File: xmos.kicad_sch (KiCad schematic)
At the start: 69 parts, among them Q1 LBSS138WT1G, Q2 BC847B, Q3 LBSS138WT1G, U10 SN74LVC125APWR, U7 XU316-1024-QF60B-C24, U8 W25Q128JVSIQ, U9 TLV73333PDBVR, Y2 24MHz

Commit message: rev2 update
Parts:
- C92: Dielectric (none) -> X5R; Supplier Part (none) -> C1525
- Q1: Manufacturer LRC(乐山无线电) -> LRC
- Q3: Current (none) -> 200mA; Manufacturer Part (none) -> LBSS138WT1G; Supplier Part (none) -> C383201
- R33: Function (none) -> XMOS; Manufacturer YAGEO -> UNI-ROYAL(Uniroyal Elec); Manufacturer Part (none) -> 0402WGF4703TCE; Supplier Part (none) -> C25790
- R34: Function (none) -> XMOS; Manufacturer YAGEO -> UNI-ROYAL(Uniroyal Elec); Manufacturer Part (none) -> 0402WGF1002TCE; Supplier Part (none) -> C25744
- R63: Function (none) -> XMOS; Manufacturer YAGEO -> UNI-ROYAL(Uniroyal Elec); Manufacturer Part (none) -> 0402WGF1000TCE; Supplier Part (none) -> C25076
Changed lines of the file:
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@@
 			)
 		)
-		(property "Manufacturer" "YAGEO"
+		(property "Manufacturer" "UNI-ROYAL(Uniroyal Elec)"
 			(at 144.78 151.13 0)
 			(effects
@@
 			)
 		)
+		(property "Manufacturer Part" "0402WGF1002TCE"
+			(at 144.78 151.13 90)
+			(effects
+				(font
+					(size 1.27 1.27)
+				)
+				(hide yes)
+			)
+		)
+		(property "Supplier Part" "C25744"
+			(at 144.78 151.13 90)
+			(effects
+				(font
+					(size 1.27 1.27)
+				)
+				(hide yes)
+			)
+		)
+		(property "Function" "XMOS"
+			(at 144.78 151.13 90)
+			(effects
+				(font
+					(size 1.27 1.27)
+				)
+				(hide yes)
+			)
+		)
 		(pin "1"
 		)
@@
 			)
 		)
-		(property "Dielectric" ""
+		(property "Dielectric" "X5R"
 			(at 144.78 165.1 0)
 			(effects
@@
 			)
 		)
+		(property "Supplier Part" "C1525"
+			(at 144.78 165.1 0)
+			(effects
+				(font
+					(size 1.27 1.27)
+				)
+				(hide yes)
+			)
+		)
 		(pin "1"
 		)
@@
 			)
 		)
-		(property "Manufacturer" "YAGEO"
+		(property "Manufacturer" "UNI-ROYAL(Uniroyal Elec)"
 			(at 107.95 165.1 0)
 			(effects
@@
 			)
 		)
+		(property "Manufacturer Part" "0402WGF1000TCE"
+			(at 107.95 165.1 0)
+			(effects
+				(font
+					(size 1.27 1.27)
+				)
+				(hide yes)
+			)
+		)
+		(property "Supplier Part" "C25076"
+			(at 107.95 165.1 0)
+			(effects
+				(font
+					(size 1.27 1.27)
+				)
+				(hide yes)
+			)
+		)
+		(property "Function" "XMOS"
+			(at 107.95 165.1 0)
+			(effects
+				(font
+					(size 1.27 1.27)
+				)
+				(hide yes)
+			)
+		)
 		(pin "1"
 		)
@@
 			)
 		)
-		(property "Manufacturer" "YAGEO"
+		(property "Manufacturer" "UNI-ROYAL(Uniroyal Elec)"
 			(at 114.3 170.18 0)
 			(effects
@@
 			)
 		)
+		(property "Manufacturer Part" "0402WGF4703TCE"
+			(at 114.3 170.18 90)
+			(effects
+				(font
+					(size 1.27 1.27)
+				)
+				(hide yes)
+			)
+		)
+		(property "Supplier Part" "C25790"
+			(at 114.3 170.18 90)
+			(effects
+				(font
+					(size 1.27 1.27)
+				)
+				(hide yes)
+			)
+		)
+		(property "Function" "XMOS"
+			(at 114.3 170.18 90)
+			(effects
+				(font
+					(size 1.27 1.27)
+				)
+				(hide yes)
+			)
+		)
 		(pin "2"
 		)
@@
 			)
 		)
-		(property "Manufacturer" "LRC(乐山无线电)"
+		(property "Manufacturer" "LRC"
 			(at 152.4 226.06 0)
 			(effects
@@
 			)
 		)
+		(property "Current" "200mA"
+			(at 124.46 165.1 0)
+			(effects
+				(font
+					(size 1.27 1.27)
+				)
+				(hide yes)
+			)
+		)
+		(property "Supplier Part" "C383201"
+			(at 124.46 165.1 0)
+			(effects
+				(font
+					(size 1.27 1.27)
+				)
+				(hide yes)
+			)
+		)
+		(property "Manufacturer Part" "LBSS138WT1G"
+			(at 124.46 165.1 0)
+			(effects
+				(font
+					(size 1.27 1.27)
+				)
+				(hide yes)
+			)
+		)

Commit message: rev2 update
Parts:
- U7: value XU316-1024-QF60B-C24 -> XU316-1024-QF60B-C32; LCSC Part # C6617472 -> C7397517; MP XU316-1024-QF60B-C24 -> XU316-1024-QF60B-C32; Manufacturer Part XU316-1024-QF60B-C24 -> XU316-1024-QF60B-C32; Supplier Part C6617472 -> C7397517
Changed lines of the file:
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@@
 			)
 		)
-		(property "Value" "XU316-1024-QF60B-C24"
+		(property "Value" "XU316-1024-QF60B-C32"
 			(at 80.01 27.94 0)
 			(effects
@@
 			)
 		)
-		(property "Datasheet" "XU316-1024-QF60B-C24"
+		(property "Datasheet" "XU316-1024-QF60B-C32"
 			(at 52.07 35.56 0)
 			(effects
@@
 			)
 		)
-		(property "MP" "XU316-1024-QF60B-C24"
+		(property "MP" "XU316-1024-QF60B-C32"
 			(at 52.07 35.56 0)
 			(effects
@@
 			)
 		)
-		(property "Supplier Part" "C6617472"
+		(property "Supplier Part" "C7397517"
 			(at 52.07 35.56 0)
 			(effects
@@
 			)
 		)
-		(property "Manufacturer Part" "XU316-1024-QF60B-C24"
+		(property "Manufacturer Part" "XU316-1024-QF60B-C32"
 			(at 52.07 35.56 0)
 			(effects
@@
 			)
 		)
-		(property "LCSC Part #" "C6617472"
+		(property "LCSC Part #" "C7397517"
 			(at 52.07 35.56 0)
 			(effects

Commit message: rev2 update
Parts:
- U7: value XU316-1024-QF60B-C32 -> XU316-1024-QF60B-C24; LCSC Part # C7397517 -> C6617472; MP XU316-1024-QF60B-C32 -> XU316-1024-QF60B-C24; Manufacturer Part XU316-1024-QF60B-C32 -> XU316-1024-QF60B-C24; Supplier Part C7397517 -> C6617472
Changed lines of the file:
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@@
 			)
 		)
-		(property "Value" "XU316-1024-QF60B-C32"
+		(property "Value" "XU316-1024-QF60B-C24"
 			(at 80.01 27.94 0)
 			(effects
@@
 			)
 		)
-		(property "Datasheet" "XU316-1024-QF60B-C32"
+		(property "Datasheet" "XU316-1024-QF60B-C24"
 			(at 52.07 35.56 0)
 			(effects
@@
 			)
 		)
-		(property "MP" "XU316-1024-QF60B-C32"
+		(property "MP" "XU316-1024-QF60B-C24"
 			(at 52.07 35.56 0)
 			(effects
@@
 			)
 		)
-		(property "Supplier Part" "C7397517"
+		(property "Supplier Part" "C6617472"
 			(at 52.07 35.56 0)
 			(effects
@@
 			)
 		)
-		(property "Manufacturer Part" "XU316-1024-QF60B-C32"
+		(property "Manufacturer Part" "XU316-1024-QF60B-C24"
 			(at 52.07 35.56 0)
 			(effects
@@
 			)
 		)
-		(property "LCSC Part #" "C7397517"
+		(property "LCSC Part #" "C6617472"
 			(at 52.07 35.56 0)
 			(effects

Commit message: rev2 update
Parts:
- C92: LCSC Part # (none) -> C1525
- Q3: LCSC Part # (none) -> C383201
- R33: value 470K -> 470k; LCSC Part # (none) -> C25790
- R34: value 10K -> 10k; LCSC Part # (none) -> C25744
- R63: LCSC Part # (none) -> C25076
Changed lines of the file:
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@@
 			)
 		)
-		(property "Value" "10K"
+		(property "Value" "10k"
 			(at 146.05 151.13 90)
 			(effects
@@
 			)
 		)
+		(property "LCSC Part #" "C25744"
+			(at 144.78 151.13 90)
+			(effects
+				(font
+					(size 1.27 1.27)
+				)
+				(hide yes)
+			)
+		)
 		(pin "1"
 		)
@@
 			)
 		)
+		(property "LCSC Part #" "C1525"
+			(at 144.78 165.1 0)
+			(effects
+				(font
+					(size 1.27 1.27)
+				)
+				(hide yes)
+			)
+		)
 		(pin "1"
 		)
@@
 			)
 		)
+		(property "LCSC Part #" "C25076"
+			(at 107.95 165.1 0)
+			(effects
+				(font
+					(size 1.27 1.27)
+				)
+				(hide yes)
+			)
+		)
 		(pin "1"
 		)
@@
 			)
 		)
-		(property "Value" "470K"
+		(property "Value" "470k"
 			(at 115.57 170.1799 90)
 			(effects
@@
 			)
 		)
+		(property "LCSC Part #" "C25790"
+			(at 114.3 170.18 90)
+			(effects
+				(font
+					(size 1.27 1.27)
+				)
+				(hide yes)
+			)
+		)
 		(pin "2"
 		)
@@
 			(at 124.46 165.1 0)
 			(effects
+				(font
+					(size 1.27 1.27)
+				)
+				(hide yes)
+			)
+		)
+		(property "LCSC Part #" "C383201"
+			(at 124.46 165.1 0)
+			(effects

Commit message: rev2 update
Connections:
- net XL_DN1: now reaches U7.33 (X1D16)
- net XL_DN0: now reaches U7.35 (X1D17)
- no-connect marks 8 -> 6
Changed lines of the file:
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@@
 	)
 	(no_connect
-		(at 107.95 116.84)
+		(at 107.95 109.22)
 	)
 	(no_connect
 		(at 107.95 73.66)
 	)
-	(no_connect
-		(at 107.95 111.76)
-	)
-	(no_connect
-		(at 107.95 109.22)
-	)
 	(wire
 		(pts
@@
 	(wire
 		(pts
+			(xy 107.95 111.76) (xy 118.11 111.76)
+		)
+		(stroke
+			(width 0)
+			(type default)
+		)
+	)
+	(wire
+		(pts
 			(xy 110.49 227.33) (xy 121.92 227.33)
 		)
@@
 		(pts
 			(xy 107.95 60.96) (xy 115.57 60.96)
+		)
+		(stroke
+			(width 0)
+			(type default)
+		)
+	)
+	(wire
+		(pts
+			(xy 107.95 116.84) (xy 118.11 116.84)
 		)
 		(stroke
@@
 		)
 	)
+	(label "XL_DN0"
+		(at 118.11 111.76 180)
+		(effects
+			(font
+				(size 1.27 1.27)
+			)
+			(justify right bottom)
+		)
+	)
 	(label "MIC_DATA_M"
 		(at 170.18 91.44 0)
@@
 		)
 	)
+	(label "XL_DN1"
+		(at 118.11 116.84 180)
+		(effects
+			(font
+				(size 1.27 1.27)
+			)
+			(justify right bottom)
+		)
+	)

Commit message: update for production
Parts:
- U8: value W25Q128JVSIQ -> W25Q32JVSSIQ; LCSC Part # C97521 -> (none); MANUFACTURER Winbond Elec -> (none); MP W25Q128JVSIQ -> (none); Manufacturer Winbond Elec -> (none); Manufacturer Part W25Q128JVSIQ -> (none); Supplier Part C97521 -> (none)
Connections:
- net ESP_IO40: no longer names the net of U7.51 (X0D43)
- net ESP_IO41: no longer names the net of U7.58 (X0D33)
- net RST_DAC: no longer names the net of U7.56 (X0D32)
- net TCK: no longer names the net of U7.24 (TCK)
- net TDI: no longer names the net of U7.18 (TDI)
- net TDO: no longer names the net of U7.20 (TDO)
- net TMS: no longer names the net of U7.23 (TMS)
- net XL_DN0: no longer names the net of U7.35 (X1D17)
- net XL_DN1: no longer names the net of U7.33 (X1D16)
- net XMOS_MUTE_DET: no longer names the net of U7.46 (X0D40)
- net XOD31: no longer names the net of U7.55 (X0D31)
- no-connect marks 6 -> 17

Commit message: complete redesign
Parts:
- removed C53: 1uF, Capacitor_SMD:C_0402_1005Metric, symbol Device:C
- removed C54, C55: 15pF, Capacitor_SMD:C_0402_1005Metric, symbol Device:C
- removed D3, D4, D5, D6, D7, D8: PESD0402V05, Diode_SMD:D_0402_1005Metric, symbol Diode:SZESD9B5.0ST5G
- removed FB4: 600R, Onju:BLM18PG121SN1D, symbol Device:FerriteBead
- removed R31: 680R, Resistor_SMD:R_0402_1005Metric, symbol Device:R
- removed R32: 1M, Resistor_SMD:R_0402_1005Metric, symbol Device:R
- removed U7: XU316-1024-QF60B-C24, Onju:XU316-1024-QF60B-C24, symbol New_Library:XU316-1024-QF60B-C24
- removed Y2: 24MHz, Crystal:Crystal_SMD_3225-4Pin_3.2x2.5mm, symbol Device:Crystal_GND24
- added C46, C52: 20pF, Capacitor_SMD:C_0402_1005Metric, symbol Seeed_libdb:Capacitors/302010050
- added C51: 1uF, Capacitor_SMD:C_0402_1005Metric, symbol Seeed_libdb:Capacitors/302013249
- added C61, C63: 100nF, Capacitor_SMD:C_0402_1005Metric, symbol Seeed_libadl:Capacitors/302010024
- added FB5: 600R, Onju:BLM18PG121SN1D, symbol Seeed_libadl:Ferrite Bead/303030521
- added J3: XTAG DEV, Connector_PinHeader_2.54mm:PinHeader_1x04_P2.54mm_Vertical, symbol Connector:Conn_01x04_Pin
- added J4: XMOS JTAG, Connector_PinHeader_2.54mm:PinHeader_2x05_P2.54mm_Vertical, symbol Connector_Generic_MountingPin:Conn_2Rows-09Pins_MountingPin
- added R30: 1M, Resistor_SMD:R_0402_1005Metric, symbol Seeed_libadl:Resistors/301010009
- added R31: 680R, Resistor_SMD:R_0402_1005Metric, symbol Seeed_libadl:Resistors/301010505
- added R33, R34: 22R, Resistor_SMD:R_0402_1005Metric, symbol Seeed_libdb:Resistors/301010002
- added R35: 100R, Resistor_SMD:R_0402_1005Metric, symbol Seeed_libdb:Resistors/301010028
- added R37, R45, R48, R49, R69, R70: 0R, Resistor_SMD:R_0402_1005Metric, symbol Seeed_libdb:Resistors/301010000
- added TP4: TEST-POINT, TestPoint:TestPoint_Pad_D1.0mm, symbol 0_Seeed_Misc:TEST-POINT
- added U8: XU316-1024-QF60B-C24​, Onju:XU316-1024-QF60B-C24, symbol reSpeaker:XU316-1024-QF60A-C24​
- added X1: 24MHz 12pF, Onju:X4-SMD-2.0X1.6MM, symbol Seeed_libdb:OSC & XTAL/306011444
- C64: renamed from C92; Dielectric X5R -> X7R; Voltage Rating 25V,X7R -> 25V
- renumbered C37 to C40, C38 to C41, C44 to C42, C39 to C43, C45 to C44, C46 to C45, C40 to C48, C48 to C49, C41 to C50, C49 to C53, C42 to C54, C50 to C55, C43 to C56, C51 to C57, C52 to C58, C59 to C65, C58 to C66, C56 to C67, C57 to C68, C60 to C69, C67 to C70, C68 to C71, C70 to C72, C69 to C73, D2 to D5, FB2 to FB4, Q3 to Q2, Q2 to Q3, R29 to R32, R30 to R41, R63 to R51, R33 to R52, R34 to R53, R50 to R54, R4 to R55, R54 to R56, R53 to R57, R51 to R58, R6 to R59, R52 to R60, R5 to R61, R11 to R62, R12 to R63, R10 to R64, R13 to R65, R55 to R66, U9 to U11, U8 to U9
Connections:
- net +1V8: now also U8.17 (VDDIOB18), U8.26 (VDDIOB18), U8.31 (USB_VDD18)
- net +3V3: now also U8.30 (USB_VDD33)
- net +5V: now also C63.1, J4.4 (Pin_4)
- net GND: now also C46.2, C51.2, C52.2, C61.2, C63.2, J4.2 (Pin_2), J4.8 (Pin_8), U8.65 (GND), X1.2, X1.4
- net I2C2_SCL: now also U8.40 (X0D29)
- net I2C2_SDA: now also U8.54 (X0D30)
- net I2C_SCL: now also R69.2
- net I2C_SDA: now also R70.2
- net I2S2_BCLK: now also R48.2
- net I2S2_DATA: now also R45.2
- net I2S2_LRCLK: now also U8.47 (X0D39)
- net I2S2_MCLK: now also R49.2
- net I2S_DIN_SEC: now also R37.2
- net MIC_CLK: now also R35.2
- net MIC_DATA: now also U8.32 (X1D13)
- net QSPI_CLK: now also U8.5 (X0D10)
- net QSPI_CS_N: now also U8.3 (X0D01)
- net QSPI_D0: now also U8.59 (X0D04)
- net QSPI_D1: now also U8.1 (X0D05)
- net QSPI_D2: now also U8.60 (X0D06)
- net QSPI_D3: now also U8.2 (X0D07)
- net RST_N: now also J4.1 (Pin_1), U8.21 (RST_N)
- net VBUS_DETEC: now also U8.11 (X1D09)
- net VDD: now also FB5.2, U8.12 (VDD), U8.19 (VDD), U8.27 (VDD), U8.34 (VDD), U8.4 (VDD), U8.42 (VDD), U8.49 (VDD), U8.57 (VDD), U8.61 (VDD), U8.62 (VDD), U8.63 (VDD), U8.64 (VDD)
- net VDDIO: now also C61.1, J4.6 (Pin_6), U8.38 (VDDIOR), U8.52 (VDDIOT), U8.8 (VDDIOL)
- new net: C52.1, R31.2, X1.3
- new net: R30.1, R31.1, U8.15 (XOUT)
- new net: C46.1, R30.2, U8.16 (XIN), X1.1
- new net: C51.1, FB5.1, U8.22 (PLL_AVDD)
- new net: R33.1, U8.36 (X1D18)
- new net: R34.1, U8.37 (X1D19)
- new net: R35.1, U8.39 (X1D22)
- new net: R48.1, U8.41 (X0D35)
- new net: R49.1, U8.43 (X0D36)
- new net: R69.1, U8.44 (X0D37)
- new net: R70.1, U8.45 (X0D38)
- new net: R45.1, U8.7 (X0D11)
- new net: R37.1, U8.9 (X1D00)
- new net SPI_CS_N: TP4.1 (T), U8.6 (X0D00)
- new net TCK: J4.7 (Pin_7), U8.24 (TCK)
- new net TDI: J4.3 (Pin_3), U8.18 (TDI)
- new net TDO: J4.5 (Pin_5), U8.20 (TDO)
- new net TMS: J4.9 (Pin_9), U8.23 (TMS)
- new net XL_DN0: J3.2 (Pin_2), U8.35 (X1D17)
- new net XL_DN1: J3.1 (Pin_1), U8.33 (X1D16)
- new net XL_UP0: J3.3 (Pin_3), R33.2
- new net XL_UP1: J3.4 (Pin_4), R34.2
- no-connect marks 17 -> 14
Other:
- title: Nest mini drop in PCB replacement -> Drop in replacement PCB for Nest mini GEN2
- moved on the sheet: C40, C41, C42, C43, C44, C45, C47, C48, C49, C50, C53, C54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

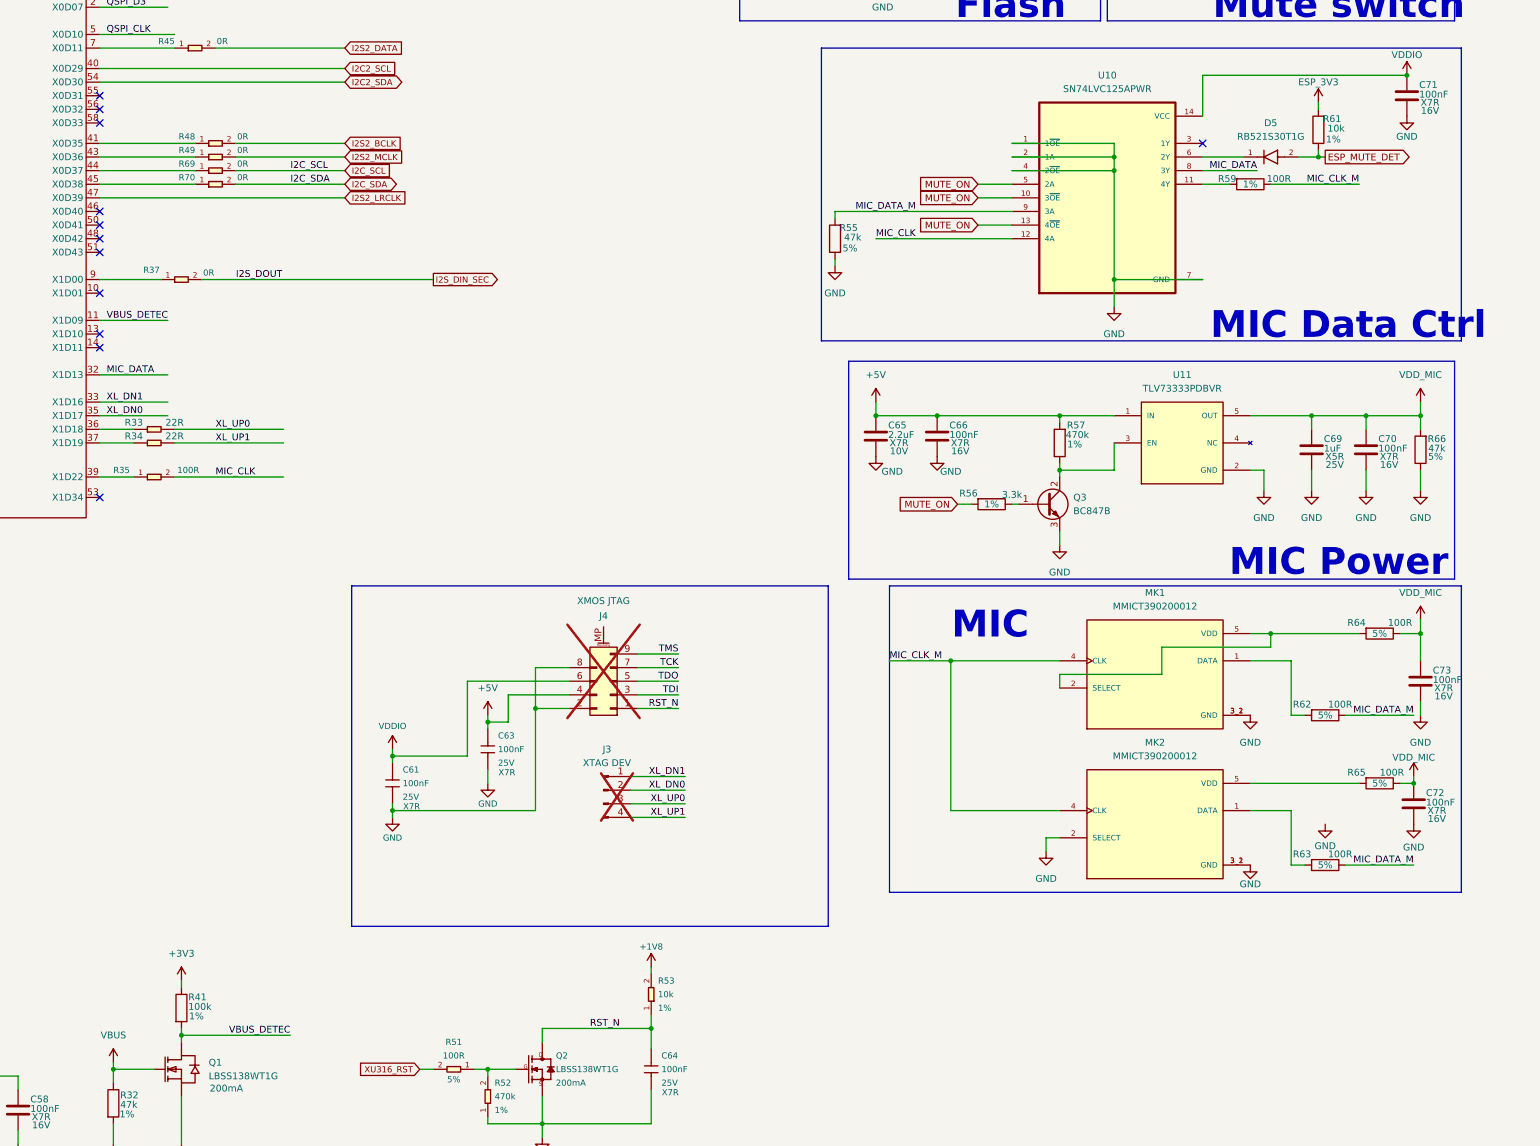
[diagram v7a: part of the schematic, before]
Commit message: preparing for the test batch
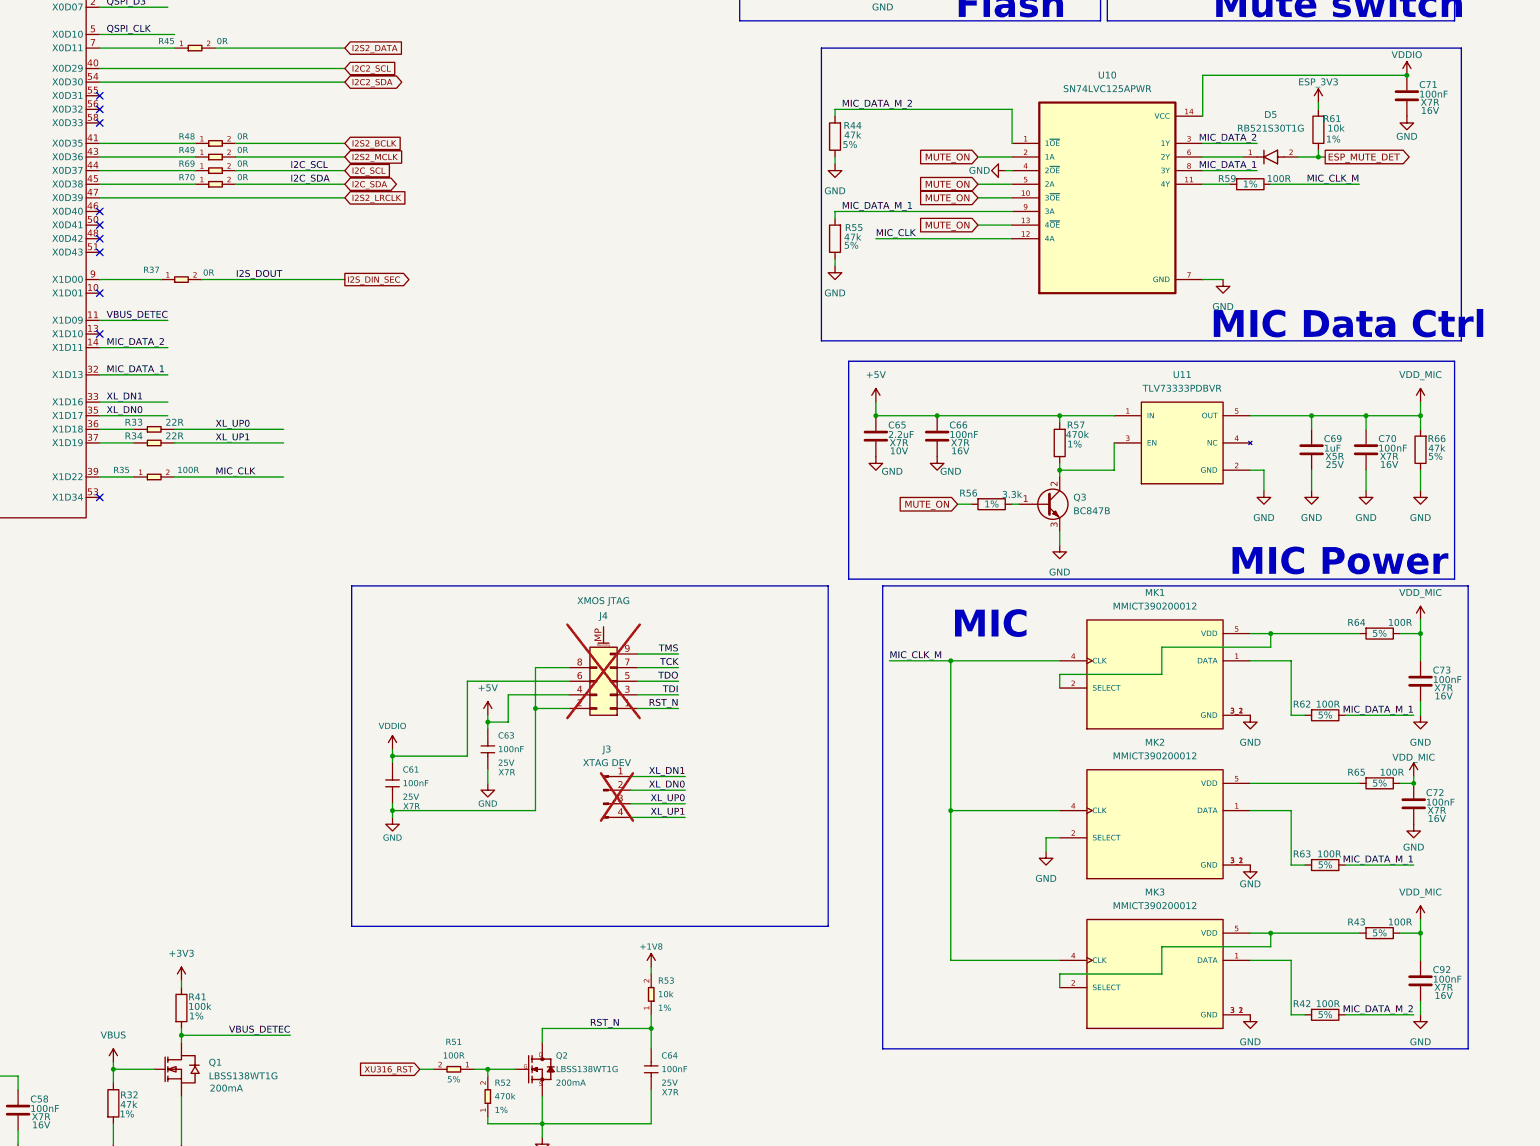
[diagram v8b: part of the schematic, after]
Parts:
- added C92: 100nF, Capacitor_SMD:C_0402_1005Metric, symbol Device:C
- added MK3: MMICT390200012, Onju:MIC_T3902, symbol New_Library:T3902
- added R42, R43: 100R, Resistor_SMD:R_0402_1005Metric, symbol Device:R
- added R44: 47k, Resistor_SMD:R_0402_1005Metric, symbol Device:R
- MK2: Availability Not in stock -> (none); Description_1 EVAL BOARD FOR MMICT390200012 -> (none)
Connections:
- net GND: now also C92.2, MK3.3_1 (GND), MK3.3_2 (GND), R44.1; no longer U10.1 (1~{OE}), U10.2 (1A)
- net MIC_CLK_M: now also MK3.4 (CLK)
- net MUTE_ON: now also U10.2 (1A)
- net VDD_MIC: now also C92.1, R43.1
- net MIC_DATA_2: now reaches U8.14 (X1D11)
- net MIC_DATA_2: now also U10.3 (1Y)
- net MIC_DATA renamed MIC_DATA_1
- net MIC_DATA_M renamed MIC_DATA_M_1
- new net: MK3.2 (SELECT), MK3.5 (VDD), R43.2
- new net: MK3.1 (DATA), R42.2
- new net MIC_DATA_M_2: R42.1, R44.2, U10.1 (1~{OE})
- no-connect marks 14 -> 12
